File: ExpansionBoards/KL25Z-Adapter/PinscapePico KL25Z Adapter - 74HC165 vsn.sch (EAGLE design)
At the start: 29 parts, among them IC1 SN74HC165DR, IC2 SN74HC165DR, IC3 SN74HC165DR, IC4 LIS3DHTR, IC5 ADS1115IDGSR, IC6 PCA9555APW,118, SW1 TS-1187A-B-A-B

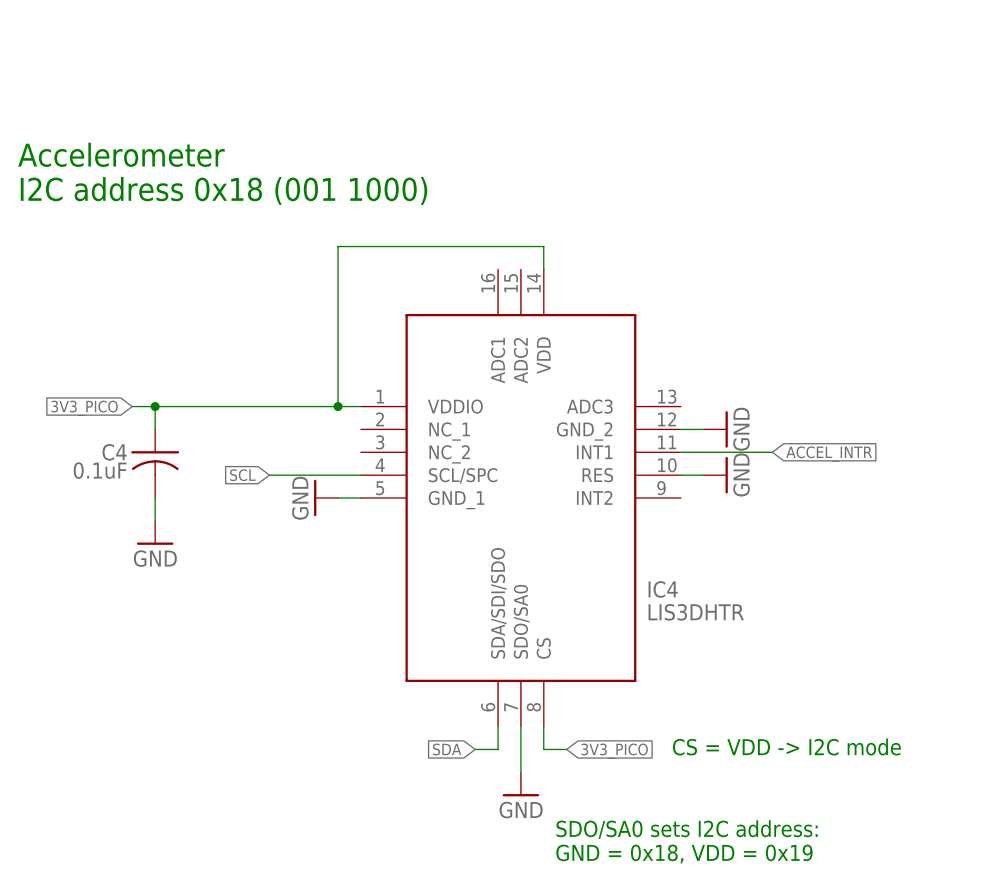
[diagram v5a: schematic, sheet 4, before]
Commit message: Update Pro and KL25Z adapter boards to make LIS3DH footprint compatible with LIS3DSH
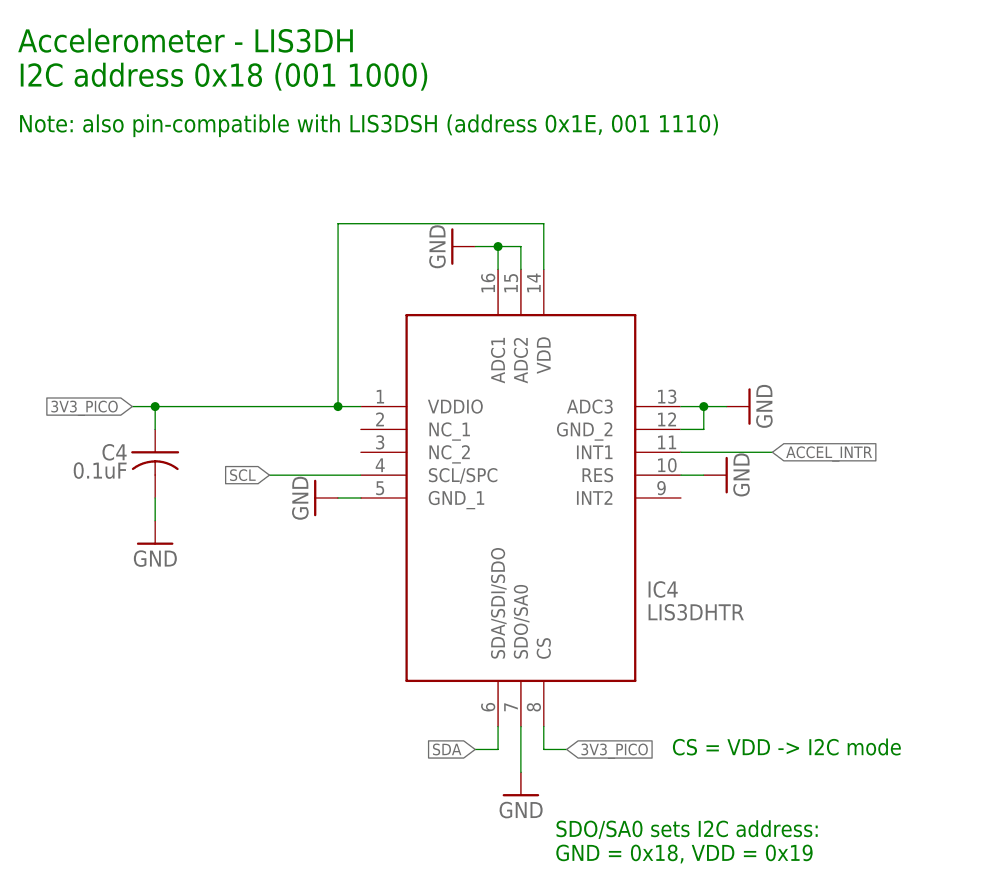
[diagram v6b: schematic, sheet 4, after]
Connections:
- net GND: now also IC4.ADC1, IC4.ADC2, IC4.ADC3
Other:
- note added: "Accelerometer - LIS3DH I2C address 0x18 (001 1000)"
- note added: "Note: also pin-compatible with LIS3DSH (address 0x1E, 001 1110)"
- note removed: "Accelerometer I2C address 0x18 (001 1000)"
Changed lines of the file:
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@@
 <part name="RN2" library="resistor-net" deviceset="CTS742C083" device=""/>
 <part name="RN3" library="resistor-net" deviceset="CTS742C083" device=""/>
+<part name="GND5" library="supply1" deviceset="GND" device=""/>
 </parts>
 <sheets>
@@
 <description>Accelerometer</description>
 <plain>
-<text x="7.62" y="73.66" size="2.54" layer="91">Accelerometer
+<text x="7.62" y="86.36" size="2.54" layer="91">Accelerometer - LIS3DH
 I2C address 0x18 (001 1000)</text>
 <text x="67.31" y="2.54" size="1.778" layer="91" align="center-left">SDO/SA0 sets I2C address:
 GND = 0x18, VDD = 0x19</text>
 <text x="80.264" y="12.954" size="1.778" layer="91" align="center-left">CS = VDD -&gt; I2C mode</text>
+<text x="7.62" y="81.28" size="1.905" layer="91">Note: also pin-compatible with LIS3DSH (address 0x1E, 001 1110)</text>
 </plain>
 <instances>
@@
 <attribute name="VALUE" x="88.9" y="45.72" size="1.778" layer="96" rot="MR270"/>
 </instance>
-<instance part="GND50" gate="1" x="86.36" y="48.26" smashed="yes" rot="MR270">
-<attribute name="VALUE" x="88.9" y="50.8" size="1.778" layer="96" rot="MR270"/>
+<instance part="GND50" gate="1" x="88.9" y="50.8" smashed="yes" rot="MR270">
+<attribute name="VALUE" x="91.44" y="53.34" size="1.778" layer="96" rot="MR270"/>
 </instance>
 <instance part="C4" gate="G$1" x="22.86" y="45.72" smashed="yes">
@@
 <instance part="GND1" gate="1" x="22.86" y="35.56" smashed="yes" rot="MR0">
 <attribute name="VALUE" x="25.4" y="33.02" size="1.778" layer="96" rot="MR0"/>
+</instance>
+<instance part="GND5" gate="1" x="55.88" y="68.58" smashed="yes" rot="MR90">
+<attribute name="VALUE" x="53.34" y="66.04" size="1.778" layer="96" rot="MR90"/>
 </instance>
 </instances>
@@
 <wire x1="81.28" y1="48.26" x2="83.82" y2="48.26" width="0.1524" layer="91"/>
 <pinref part="GND50" gate="1" pin="GND"/>
+<pinref part="IC4" gate="G$1" pin="ADC3"/>
+<wire x1="81.28" y1="50.8" x2="83.82" y2="50.8" width="0.1524" layer="91"/>
+<wire x1="83.82" y1="50.8" x2="86.36" y2="50.8" width="0.1524" layer="91"/>
+<wire x1="83.82" y1="50.8" x2="83.82" y2="48.26" width="0.1524" layer="91"/>
+<junction x="83.82" y="50.8"/>
 </segment>
 <segment>
@@
 <wire x1="22.86" y1="40.64" x2="22.86" y2="38.1" width="0.1524" layer="91"/>
 <pinref part="GND1" gate="1" pin="GND"/>
+</segment>
+<segment>
+<pinref part="IC4" gate="G$1" pin="ADC2"/>
+<wire x1="63.5" y1="66.04" x2="63.5" y2="68.58" width="0.1524" layer="91"/>
+<wire x1="63.5" y1="68.58" x2="60.96" y2="68.58" width="0.1524" layer="91"/>
+<pinref part="IC4" gate="G$1" pin="ADC1"/>
+<wire x1="60.96" y1="68.58" x2="60.96" y2="66.04" width="0.1524" layer="91"/>
+<wire x1="60.96" y1="68.58" x2="58.42" y2="68.58" width="0.1524" layer="91"/>
+<junction x="60.96" y="68.58"/>
+<pinref part="GND5" gate="1" pin="GND"/>
 </segment>
 </net>
@@
 <wire x1="43.18" y1="50.8" x2="22.86" y2="50.8" width="0.1524" layer="91"/>
 <wire x1="22.86" y1="50.8" x2="20.32" y2="50.8" width="0.1524" layer="91"/>
-<wire x1="66.04" y1="66.04" x2="66.04" y2="68.58" width="0.1524" layer="91"/>
-<wire x1="66.04" y1="68.58" x2="43.18" y2="68.58" width="0.1524" layer="91"/>
-<wire x1="43.18" y1="68.58" x2="43.18" y2="50.8" width="0.1524" layer="91"/>
+<wire x1="66.04" y1="66.04" x2="66.04" y2="71.12" width="0.1524" layer="91"/>
+<wire x1="66.04" y1="71.12" x2="43.18" y2="71.12" width="0.1524" layer="91"/>
+<wire x1="43.18" y1="71.12" x2="43.18" y2="50.8" width="0.1524" layer="91"/>
 <junction x="43.18" y="50.8"/>
 <label x="20.32" y="50.8" size="1.27" layer="95" rot="R180" xref="yes"/>

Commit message: PCB parts lists (BOMs); power distro board edits
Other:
- note added: "Copyright and License Info Pinscape Pico Adapter Board for Pinscape-KL25Z Expansion Set Copyright 2024, 2025 Michael J Roberts BSD 3-clause license"
- note added: "EC3203ARGB: Vf @ 5mA: R 1.8, G 2.8, B 2.8 -> R3 (R) 360, R2 (G) 100, R1 (B) 100 Pin-compatible substitutes: Wurth 150141M173100 Vf: R 2V @ 10mA, G 3.0V @ 8mA, B 3.0V @ 10mA -> R3 (R) 130, R2 (G) 39, R1 (B) 30"
